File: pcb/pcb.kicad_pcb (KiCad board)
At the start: 2 copper layers, 63 x 56 mm, 18 parts

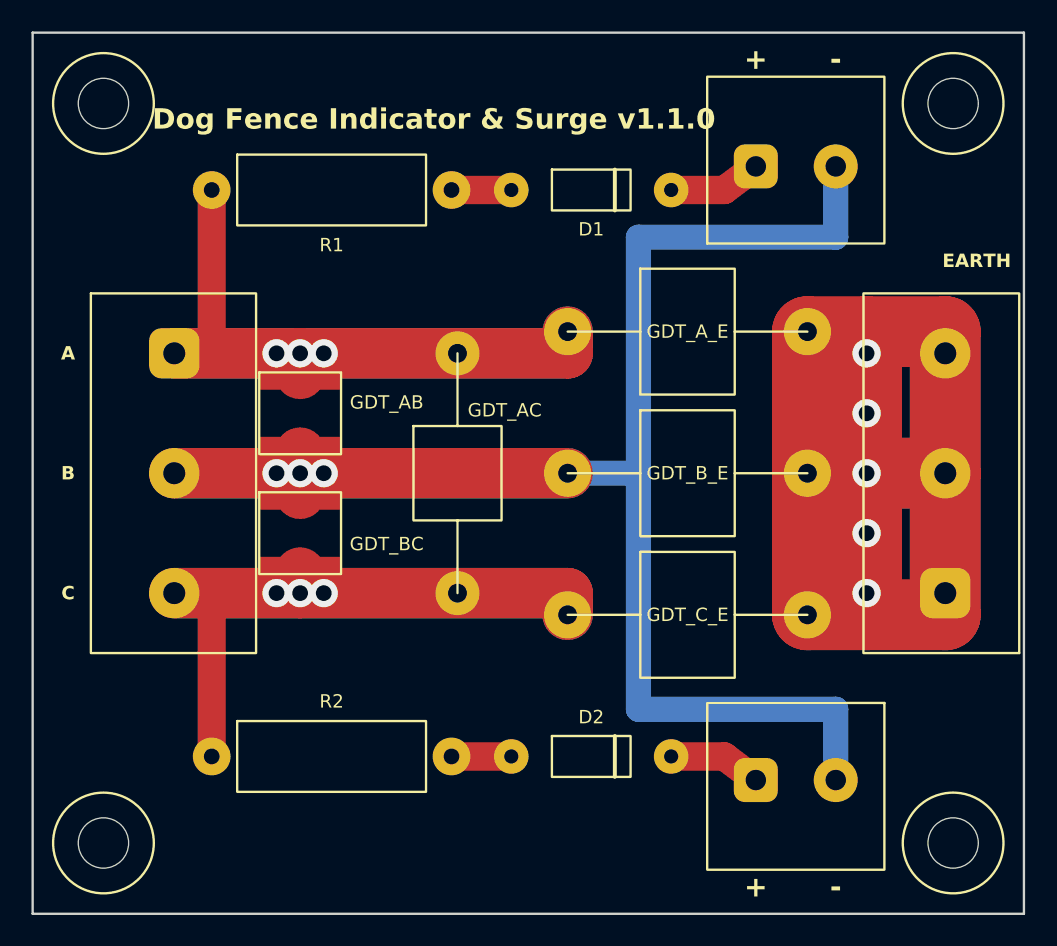
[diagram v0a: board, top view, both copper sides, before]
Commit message: Clean up schematic to align with PCB
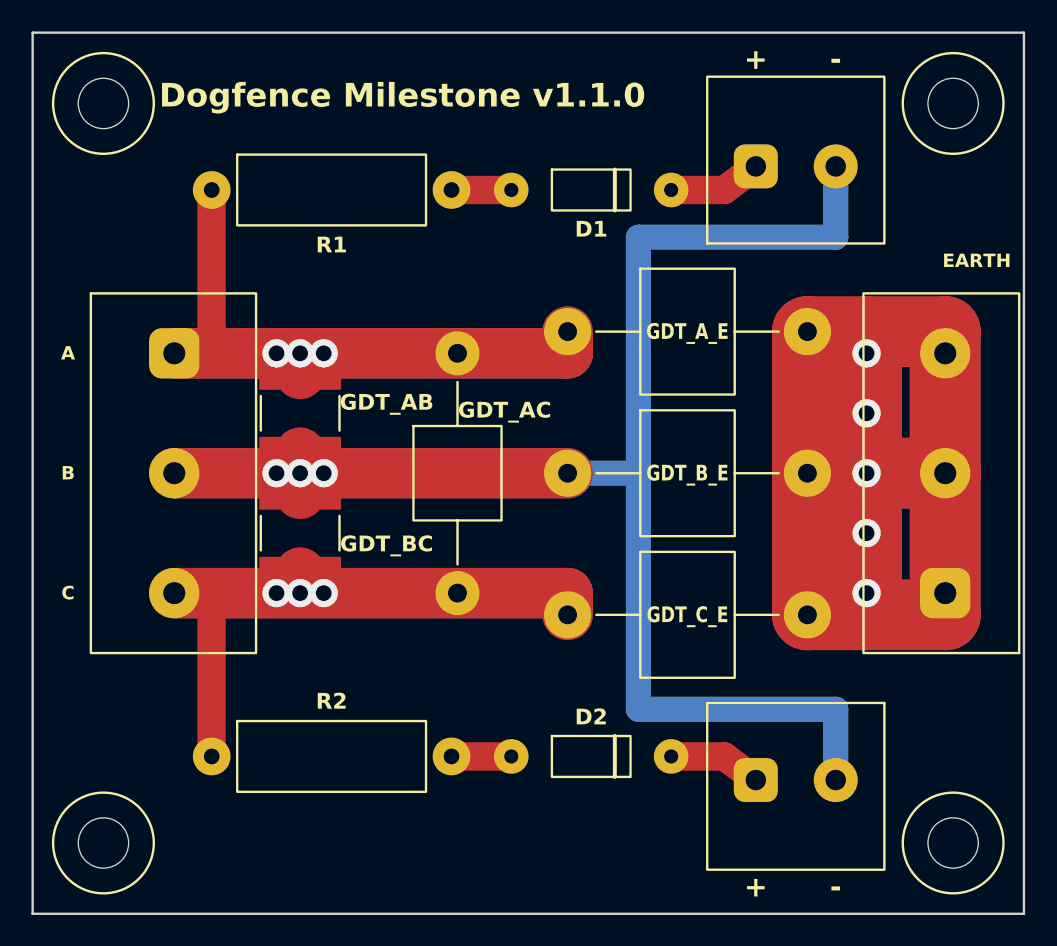
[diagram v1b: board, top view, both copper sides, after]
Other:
- board text added: "Dogfence Milestone v1.1.0"
- board text removed: "Dog Fence Indicator & Surge v1.1.0"

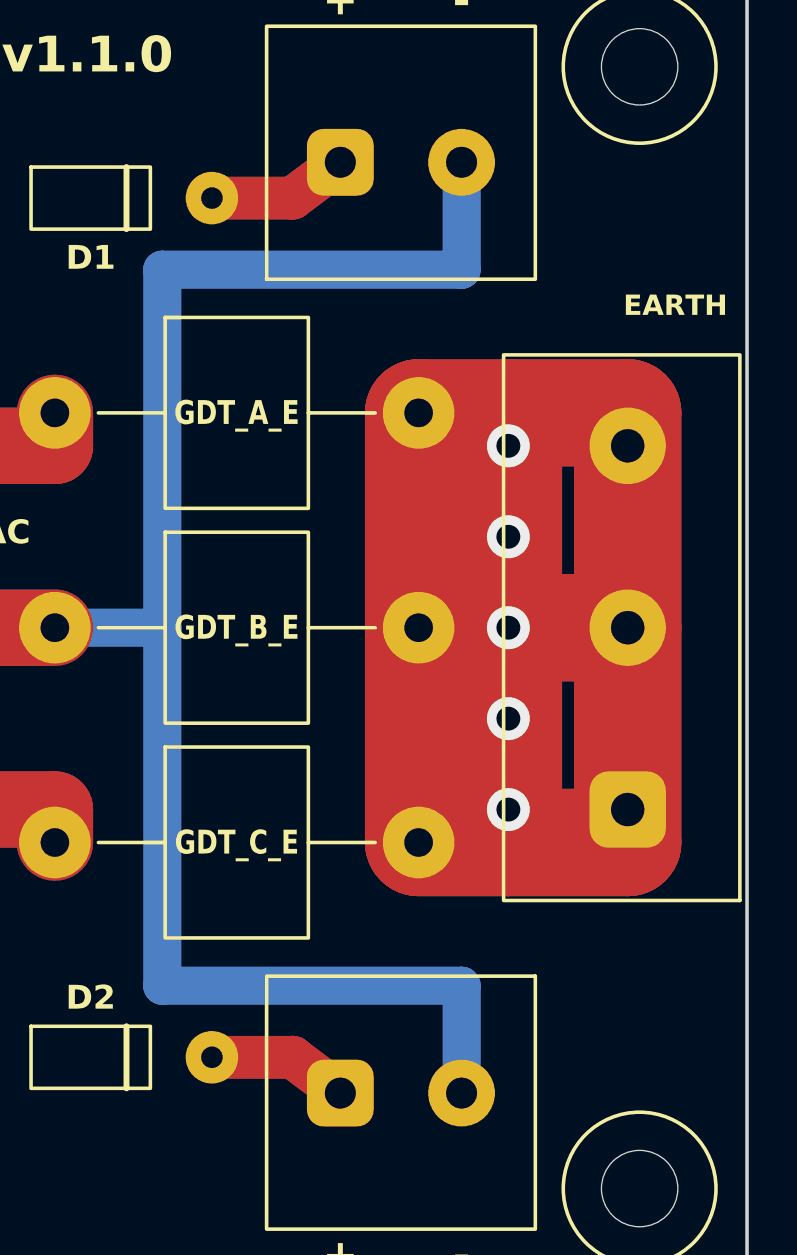
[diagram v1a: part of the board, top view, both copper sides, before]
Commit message: Improve EARTH front and back side design
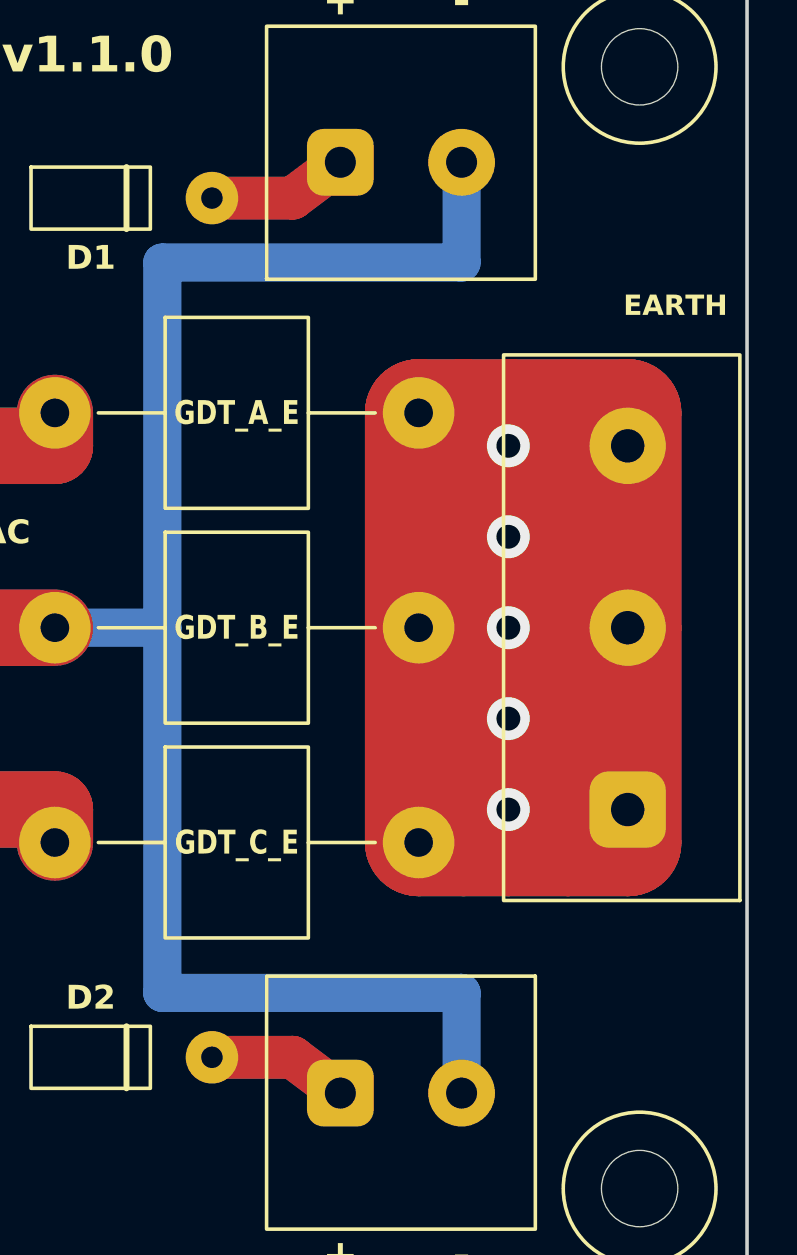
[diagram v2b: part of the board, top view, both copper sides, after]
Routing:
- net EARTH: track 160.6 -> 232.6 mm
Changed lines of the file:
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@@
 	)
 	(segment
-		(start 135.5 107.5)
-		(end 148.04 107.5)
-		(width 1.6)
-		(layer "B.Cu")
-		(net 2)
-	)
-	(segment
-		(start 148.04 107.5)
+		(start 135.5 107.2)
+		(end 148.04 107.2)
+		(width 1.6)
+		(layer "B.Cu")
+		(net 2)
+	)
+	(segment
+		(start 148.04 107.2)
 		(end 148.04 103)
 		(width 1.6)
@@
 	(segment
 		(start 135.5 122.5)
-		(end 135.5 137.5)
+		(end 135.5 137.8)
 		(width 1.6)
 		(layer "B.Cu")
@@
 	)
 	(segment
-		(start 148.04 137.5)
+		(start 148.04 137.8)
 		(end 148.04 142)
 		(width 1.6)
@@
 	(segment
 		(start 135.5 122.5)
-		(end 135.5 107.5)
-		(width 1.6)
-		(layer "B.Cu")
-		(net 2)
-	)
-	(segment
-		(start 135.5 137.5)
-		(end 148.04 137.5)
+		(end 135.5 107.2)
+		(width 1.6)
+		(layer "B.Cu")
+		(net 2)
+	)
+	(segment
+		(start 135.5 137.8)
+		(end 148.04 137.8)
 		(width 1.6)
 		(layer "B.Cu")
@@
 	)
 	(segment
-		(start 146.24 131.5)
-		(end 155 131.5)
+		(start 146.24 113.5)
+		(end 146.24 131.5)
+		(width 4.5)
+		(layer "F.Cu")
+		(net 4)
+	)
+	(segment
+		(start 148.12 113.5)
+		(end 148.12 131.5)
+		(width 4.5)
+		(layer "F.Cu")
+		(net 4)
+	)
+	(segment
+		(start 150 113.5)
+		(end 150 131.5)
+		(width 4.5)
+		(layer "F.Cu")
+		(net 4)
+	)
+	(segment
+		(start 152.5 113.5)
+		(end 152.5 131.5)
+		(width 4.5)
+		(layer "F.Cu")
+		(net 4)
+	)
+	(segment
+		(start 155 113.5)
+		(end 155 131.5)
+		(width 4.5)
+		(layer "F.Cu")
+		(net 4)
+	)
+	(segment
+		(start 146.24 113.5)
+		(end 155 113.5)
 		(width 4.5)
 		(layer "F.Cu")
@@
 	)
 	(segment
-		(start 155 113.5)
-		(end 155 131.5)
-		(width 4.5)
-		(layer "F.Cu")
-		(net 4)
-	)
-	(segment
-		(start 146.24 113.5)
-		(end 155 113.5)
-		(width 4.5)
-		(layer "F.Cu")
+		(start 146.24 131.5)
+		(end 155 131.5)
+		(width 4.5)
+		(layer "F.Cu")
+		(net 4)
+	)
+	(via
+		(at 150 126.31)
+		(size 1.8)
+		(drill 1)
+		(layers "F.Cu" "B.Cu")
+		(net 4)
+	)
+	(via
+		(at 150 114.88)
+		(size 1.8)
+		(drill 1)
+		(layers "F.Cu" "B.Cu")
+		(net 4)
+	)
+	(via
+		(at 150 122.5)
+		(size 1.8)
+		(drill 1)
+		(layers "F.Cu" "B.Cu")
+		(net 4)
+	)
+	(via
+		(at 150 118.69)
+		(size 1.8)
+		(drill 1)
+		(layers "F.Cu" "B.Cu")
+		(net 4)
+	)
+	(via
+		(at 150 130.12)
+		(size 1.8)
+		(drill 1)
+		(layers "F.Cu" "B.Cu")
 		(net 4)
 	)
@@
 		(end 146.24 131.5)
 		(width 4.5)
-		(layer "F.Cu")
+		(layer "B.Cu")
+		(net 4)
+	)
+	(segment
+		(start 148.12 113.5)
+		(end 148.12 131.5)
+		(width 4.5)
+		(layer "B.Cu")
 		(net 4)
 	)
@@
 		(end 150 131.5)
 		(width 4.5)
-		(layer "F.Cu")
-		(net 4)
-	)
-	(via
-		(at 150 126.31)
-		(size 1.8)
-		(drill 1)
-		(layers "F.Cu" "B.Cu")
-		(net 4)
-	)
-	(via
-		(at 150 114.88)
-		(size 1.8)
-		(drill 1)
-		(layers "F.Cu" "B.Cu")
-		(net 4)
-	)
-	(via
-		(at 150 122.5)
-		(size 1.8)
-		(drill 1)
-		(layers "F.Cu" "B.Cu")
-		(net 4)
-	)
-	(via
-		(at 150 118.69)
-		(size 1.8)
-		(drill 1)
-		(layers "F.Cu" "B.Cu")
-		(net 4)
-	)
-	(via
-		(at 150 130.12)
-		(size 1.8)
-		(drill 1)
-		(layers "F.Cu" "B.Cu")
+		(layer "B.Cu")
+		(net 4)
+	)
+	(segment
+		(start 152.5 113.5)
+		(end 152.5 131.5)
+		(width 4.5)
+		(layer "B.Cu")
+		(net 4)
+	)
+	(segment
+		(start 155 113.5)
+		(end 155 131.5)
+		(width 4.5)
+		(layer "B.Cu")
 		(net 4)
 	)
@@
 		(start 146.24 113.5)
 		(end 155 113.5)
-		(width 3)
-		(layer "B.Cu")
-		(net 4)
-	)
-	(segment
-		(start 150 113.5)
-		(end 150 131.5)
-		(width 4.5)
-		(layer "B.Cu")
-		(net 4)
-	)
-	(segment
-		(start 146.24 113.5)
-		(end 146.24 131.5)
-		(width 3)
-		(layer "B.Cu")
-		(net 4)
-	)
-	(segment
-		(start 146.24 131.5)
-		(end 155 131.5)
-		(width 3)
-		(layer "B.Cu")
-		(net 4)
-	)
-	(segment
-		(start 155 113.5)
-		(end 155 131.5)
 		(width 4.5)
 		(layer "B.Cu")
@@
 		(width 4.5)
 		(layer "B.Cu")
+		(net 4)
+	)
+	(segment
+		(start 146.24 131.5)
+		(end 155 131.5)
+		(width 4.5)
+		(layer "B.Cu")

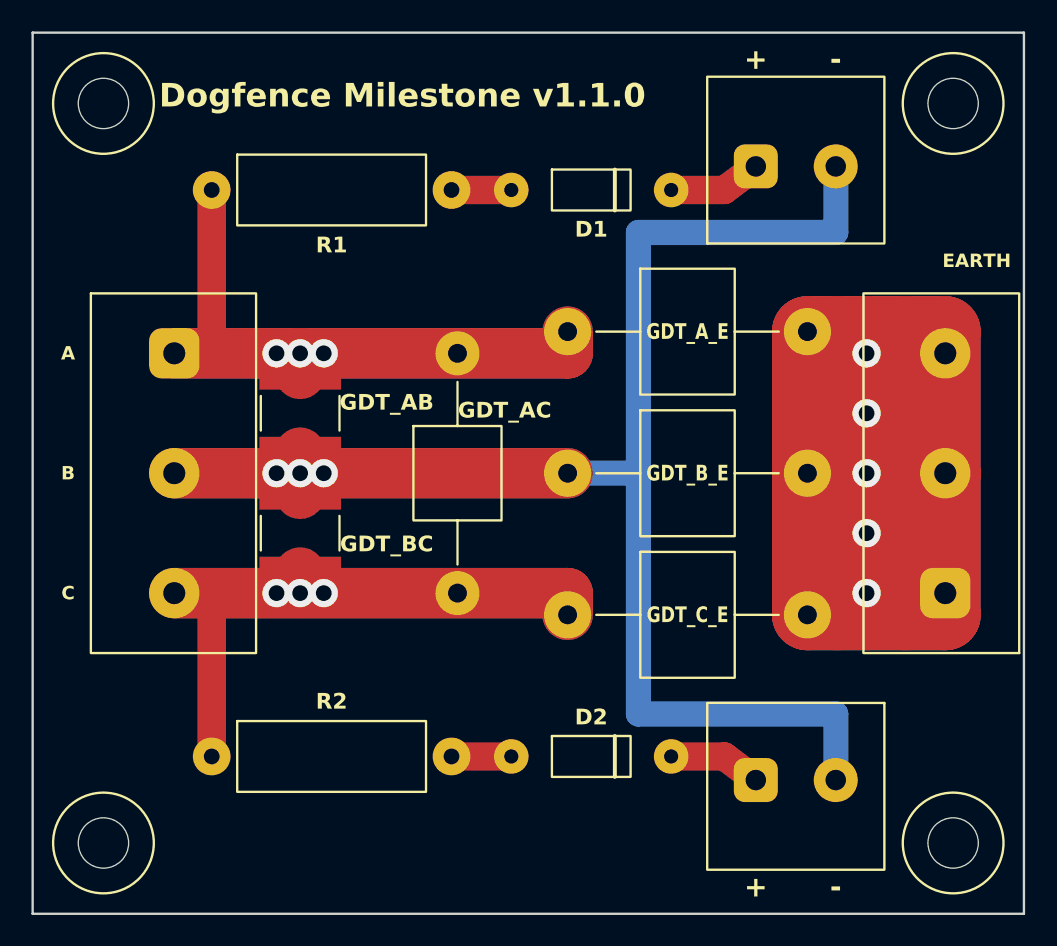
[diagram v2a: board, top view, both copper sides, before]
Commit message: Implement guarded remediation and manufacturing verification
Add complete-project checks, native manufacturing validation, electrical regressions, and bounded PCB/library corrections for 1.2.0-dev. Preserve unresolved protection, fit/process, and hardware qualification holds.
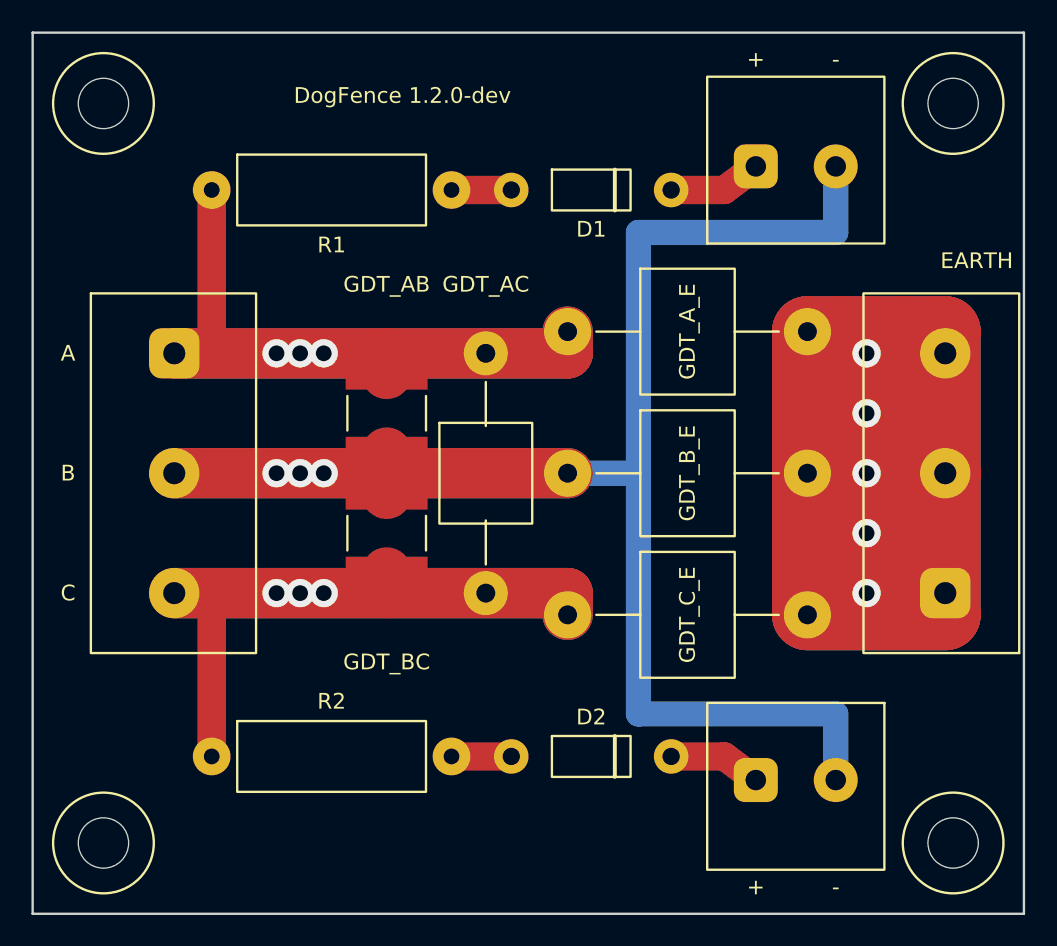
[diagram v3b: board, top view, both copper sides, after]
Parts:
- D1, D2: footprint Diode_THT:D_DO-41_SOD81_P10.16mm_Horizontal -> DogFence:1N4007G_P10.16mm_K_Right
- GDT_AB, GDT_BC: footprint GDT_SMD:GDT_SMD_5.0x5.0mm -> DogFence:SMD5050-470NA
- GDT_AC: footprint Resistor_THT:R_Axial_DIN0617_L17.0mm_D6.0mm_P15.24mm_Horizontal -> DogFence:B5G470L_P15.24mm_NS_Overpass
- GDT_A_E, GDT_B_E, GDT_C_E: footprint Resistor_THT:R_Axial_DIN0617_L17.0mm_D6.0mm_P15.24mm_Horizontal -> DogFence:2R470TD-8_P15.24mm
- H1, H2, H3, H4: value MountingHole_3.2mm_M3 -> MountingHole_3.2mm; footprint MountingHole:MountingHole_3.2mm_M3 -> DogFence:MountingHole_3.2mm
- J_EARTH: footprint TerminalBlock_Phoenix:TerminalBlock_Phoenix_MKDS-1,5-3-7.62_1x03_P7.62mm_Horizontal -> DogFence:KF128_7.62_3P_Earth
- J_IN: footprint TerminalBlock_Phoenix:TerminalBlock_Phoenix_MKDS-1,5-3-7.62_1x03_P7.62mm_Horizontal -> DogFence:KF128_7.62_3P_Input
- J_LED_A: footprint TerminalBlock_Phoenix:TerminalBlock_Phoenix_MKDS-1,5-2-5.08_1x02_P5.08mm_Horizontal -> DogFence:KF129_5.08_2P_LED_A
- J_LED_C: footprint TerminalBlock_Phoenix:TerminalBlock_Phoenix_MKDS-1,5-2-5.08_1x02_P5.08mm_Horizontal -> DogFence:KF129_5.08_2P_LED_C
- R1, R2: footprint Resistor_THT:R_Axial_DIN0414_L11.9mm_D4.5mm_P15.24mm_Horizontal -> DogFence:MBE0414_P15.24mm
- moved GDT_AB 5.50 mm to (119.5, 118.7)
- moved GDT_BC 5.50 mm to (119.5, 126.3)
- moved GDT_AC 1.80 mm to (125.8, 122.5)
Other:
- board text added: "DogFence 1.2.0-dev"
- board text removed: "Dogfence Milestone v1.1.0"
